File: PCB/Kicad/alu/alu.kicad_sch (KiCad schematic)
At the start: 2 parts

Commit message: Update
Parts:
- removed REF2, REF3: ~, mALUch_lib:PinHeader_2x20_P2.54mm_Horizontal, symbol mALUch_lib:2x20_2.54_Horizontal
- added J1: Conn_02x10_Odd_Even, symbol Connector_Generic:Conn_02x10_Odd_Even
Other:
- removed sheet 16b AND
- removed sheet 16b LSL
- removed sheet 16b LSR
- removed sheet 16b NOT
- removed sheet 16b OR
- removed sheet 16b XOR
- removed sheet 16b fulladder
- removed sheet 16b fulladder1
- removed sheet ALU MUX
- added sheet ADD_SUB (ADD_SUB.kicad_sch)
- added sheet AND (AND.kicad_sch)
- added sheet DECODE (DECODE.kicad_sch)
- added sheet NOT (NOT.kicad_sch)
- added sheet OR (OR.kicad_sch)
- added sheet OUT_EN (OUT_EN.kicad_sch)
- added sheet REGISTER (REGISTER.kicad_sch)
- added sheet SHIFT_REG (SHIFT_REG.kicad_sch)
- added sheet XOR (XOR.kicad_sch)
- company: AGH Logic Unit -> (none)
- title: Arithmetic Logic Unit -> (none)

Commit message: UPDATE
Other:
- sheet DECODE ports: added OP[0..3], ~{EN}, ~{REG_LOAD}, ~{SEL_ADD}, ~{SEL_AND}, ~{SEL_NOT}, ~{SEL_OR}, ~{SEL_SHL}, ~{SEL_SHR}, ~{SEL_SUB}, ~{SEL_XOR}; removed none
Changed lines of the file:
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@@
 	)
 	(sheet
-		(at 82.55 93.98)
-		(size 12.7 3.81)
+		(at 105.41 83.82)
+		(size 12.7 50.8)
 		(exclude_from_sim no)
 		(in_bom yes)
@@
 		)
 		(property "Sheetname" "DECODE"
-			(at 82.55 93.2684 0)
+			(at 105.41 83.1084 0)
 			(effects
 				(font
@@
 		)
 		(property "Sheetfile" "DECODE.kicad_sch"
-			(at 82.55 98.3746 0)
+			(at 105.41 135.2046 0)
 			(effects
 				(font
@@
 				)
 				(justify left top)
+			)
+		)
+		(pin "OP[0..3]" input
+			(at 105.41 85.09 180)
+			(effects
+				(font
+					(size 1.27 1.27)
+				)
+				(justify left)
+			)
+		)
+		(pin "~{EN}" input
+			(at 105.41 88.9 180)
+			(effects
+				(font
+					(size 1.27 1.27)
+				)
+				(justify left)
+			)
+		)
+		(pin "~{REG_LOAD}" output
+			(at 118.11 133.35 0)
+			(effects
+				(font
+					(size 1.27 1.27)
+				)
+				(justify right)
+			)
+		)
+		(pin "~{SEL_ADD}" output
+			(at 118.11 121.92 0)
+			(effects
+				(font
+					(size 1.27 1.27)
+				)
+				(justify right)
+			)
+		)
+		(pin "~{SEL_AND}" output
+			(at 118.11 106.68 0)
+			(effects
+				(font
+					(size 1.27 1.27)
+				)
+				(justify right)
+			)
+		)
+		(pin "~{SEL_NOT}" output
+			(at 118.11 110.49 0)
+			(effects
+				(font
+					(size 1.27 1.27)
+				)
+				(justify right)
+			)
+		)
+		(pin "~{SEL_OR}" output
+			(at 118.11 102.87 0)
+			(effects
+				(font
+					(size 1.27 1.27)
+				)
+				(justify right)
+			)
+		)
+		(pin "~{SEL_SHL}" output
+			(at 118.11 125.73 0)
+			(effects
+				(font
+					(size 1.27 1.27)
+				)
+				(justify right)
+			)
+		)
+		(pin "~{SEL_SHR}" output
+			(at 118.11 129.54 0)
+			(effects
+				(font
+					(size 1.27 1.27)
+				)
+				(justify right)
+			)
+		)
+		(pin "~{SEL_SUB}" output
+			(at 118.11 118.11 0)
+			(effects
+				(font
+					(size 1.27 1.27)
+				)
+				(justify right)
+			)
+		)
+		(pin "~{SEL_XOR}" output
+			(at 118.11 114.3 0)
+			(effects
+				(font
+					(size 1.27 1.27)
+				)
+				(justify right)
 			)
 		)
@@
 	)
 	(sheet
-		(at 81.28 46.99)
+		(at 105.41 40.64)
 		(size 17.78 15.24)
 		(exclude_from_sim no)
@@
 		)
 		(property "Sheetname" "REGISTER"
-			(at 81.28 46.2784 0)
+			(at 105.41 39.9284 0)
 			(effects
 				(font
@@
 		)
 		(property "Sheetfile" "REGISTER.kicad_sch"
-			(at 81.28 62.8146 0)
+			(at 105.41 56.4646 0)
 			(effects
 				(font
@@
 		)
 		(pin "CLK" input
-			(at 81.28 53.34 180)
+			(at 105.41 46.99 180)
 			(effects
 				(font
@@
 		)
 		(pin "REG_IN[0..15]" input
-			(at 81.28 49.53 180)
+			(at 105.41 43.18 180)
 			(effects
 				(font
@@
 		)
 		(pin "REG_OUT[0..15]" output
-			(at 99.06 59.69 0)
+			(at 123.19 53.34 0)
 			(effects
 				(font
@@
 		)
 		(pin "~{REG_EN}" input
-			(at 81.28 57.15 180)
+			(at 105.41 50.8 180)
 			(effects
 				(font
@@
 	)
 	(sheet
-		(at 81.28 68.58)
+		(at 105.41 62.23)
 		(size 12.7 15.24)
 		(exclude_from_sim no)
@@
 		)
 		(property "Sheetname" "OUT_EN"
-			(at 81.28 67.8684 0)
+			(at 105.41 61.5184 0)
 			(effects
 				(font
@@
 		)
 		(property "Sheetfile" "OUT_EN.kicad_sch"
-			(at 81.28 84.4046 0)
+			(at 105.41 78.0546 0)
 			(effects
 				(font
@@
 		)
 		(pin "IN[0..15]" input
-			(at 81.28 71.12 180)
+			(at 105.41 64.77 180)
 			(effects
 				(font
@@
 		)
 		(pin "OUT[0..15]" output
-			(at 93.98 81.28 0)
+			(at 118.11 74.93 0)
 			(effects
 				(font
@@
 		)
 		(pin "~{CE}" input
-			(at 81.28 74.93 180)
-			(effects
-				(font
+			(at 105.41 68.58 180)
+			(effects
+				(font

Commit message: UPDATE
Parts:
- added J2: Conn_02x10_Odd_Even, symbol Connector_Generic:Conn_02x10_Odd_Even
- added U51: 74LS04, symbol 74xx:74LS04
- added U68: 74LS08, symbol 74xx:74LS08
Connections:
- net ADD_SUB/IS_SUB: now also U51.12
- net SHIFT_REG/REV: now also U51.10
- net PWR: now reaches J1.1 (Pin_1)
- net PWR: now also J1.19 (Pin_19), J2.1 (Pin_1), J2.19 (Pin_19)
- net GND: now reaches J1.10 (Pin_10)
- net GND: now also J1.12 (Pin_12), J1.16 (Pin_16), J1.2 (Pin_2), J1.20 (Pin_20), J1.6 (Pin_6), J2.14 (Pin_14), J2.16 (Pin_16), J2.2 (Pin_2), J2.20 (Pin_20), J2.8 (Pin_8), U51.7 (GND), U68.7 (GND)
- net D11: now reaches J1.11 (Pin_11)
- net D10: now reaches J1.13 (Pin_13)
- net OP1: now reaches J1.14 (Pin_14)
- net D09: now reaches J1.15 (Pin_15)
- net D08: now reaches J1.17 (Pin_17)
- net OP0: now reaches J1.18 (Pin_18)
- net D15: now reaches J1.3 (Pin_3)
- net OP3: now reaches J1.4 (Pin_4)
- net D14: now reaches J1.5 (Pin_5)
- net D13: now reaches J1.7 (Pin_7)
- net OP2: now reaches J1.8 (Pin_8)
- net D12: now reaches J1.9 (Pin_9)
- new net CLK: J2.18 (Pin_18)
- new net D00: J2.17 (Pin_17)
- new net D01: J2.15 (Pin_15)
- new net D02: J2.13 (Pin_13)
- new net D03: J2.11 (Pin_11)
- new net D04: J2.9 (Pin_9)
- new net D05: J2.7 (Pin_7)
- new net D06: J2.5 (Pin_5)
- new net D07: J2.3 (Pin_3)
- new net FC: J2.10 (Pin_10)
- new net FO: J2.6 (Pin_6)
- new net FS: J2.4 (Pin_4)
- new net FZ: J2.12 (Pin_12)
- new net VCC: U51.14 (VCC), U68.14 (VCC)
- new net ~{SEL_ADD_SUB}: U68.11
- new net ~{SEL_ADD}: U68.13
- new net ~{SEL_SHIFT}: U68.8
- new net ~{SEL_SHL}: U68.9
- new net ~{SEL_SHR}: U51.11, U68.10
- new net ~{SEL_SUB}: U51.13, U68.12
- no-connect marks 0 -> 14
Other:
- sheet REGISTER renamed REG_A
- added sheet GATE_ADD (OUT_EN.kicad_sch)
- added sheet GATE_AND (OUT_EN.kicad_sch)
- added sheet GATE_NOT (OUT_EN.kicad_sch)
- added sheet GATE_OR (OUT_EN.kicad_sch)
- added sheet GATE_SHIFT (OUT_EN.kicad_sch)
- added sheet GATE_XOR (OUT_EN.kicad_sch)
- added sheet REG_B (REGISTER.kicad_sch)
- sheet DECODE ports: added ~{LOAD_A_REG}, ~{LOAD_B_REG}; removed ~{REG_LOAD}
- note added: "Verify the shift direction"
- moved on the sheet: J1

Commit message: UPDATE
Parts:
- removed U51: 74LS04, symbol 74xx:74LS04
- added C1: 10n, symbol Device:C
- added D1: Green LED, symbol Device:LED
- added D2, D3, D4, D5: Yellow LED, symbol Device:LED
- added R1, R2, R3, R4, R5: 680, symbol Device:R
- added U9: 74LS04, symbol 74xx:74LS04
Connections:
- net FS is gone; now on net D15: J2.4 (Pin_4)
- net PWR is gone; now on net VCC: J1.1 (Pin_1), J1.19 (Pin_19), J2.1 (Pin_1), J2.19 (Pin_19)
- net D15: now also R4.1
- net FC: now also R5.1
- net FO: now also R2.1
- net FZ: now also R3.1
- net GND: now also C1.2, D1.1 (K), D2.1 (K), D3.1 (K), D4.1 (K), D5.1 (K)
- net SHIFT_REG/REV: now also U9.12
- net VCC: now also C1.1, R1.1
- net ~{SEL_SHR}: now also U9.13
- net ~{SEL_SUB}: now also U9.11
- net D00 renamed D0
- net D01 renamed D1
- net D02 renamed D2
- net D03 renamed D3
- net D04 renamed D4
- net D05 renamed D5
- net D06 renamed D6
- net D07 renamed D7
- net D08 renamed D8
- net D09 renamed D9
- new net: D3.2 (A), R3.2
- new net: D4.2 (A), R4.2
- new net: D2.2 (A), R2.2
- new net: D5.2 (A), R5.2
- new net: D1.2 (A), R1.2
- new net IS_SUB: U9.10
- no-connect marks 14 -> 6
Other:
- removed sheet OUT_EN
- added sheet FO_FZ (OVERFLOW_FLAG.kicad_sch)
- sheet ADD_SUB ports: added FC; removed none
- moved on the sheet: J1, J2, U68E

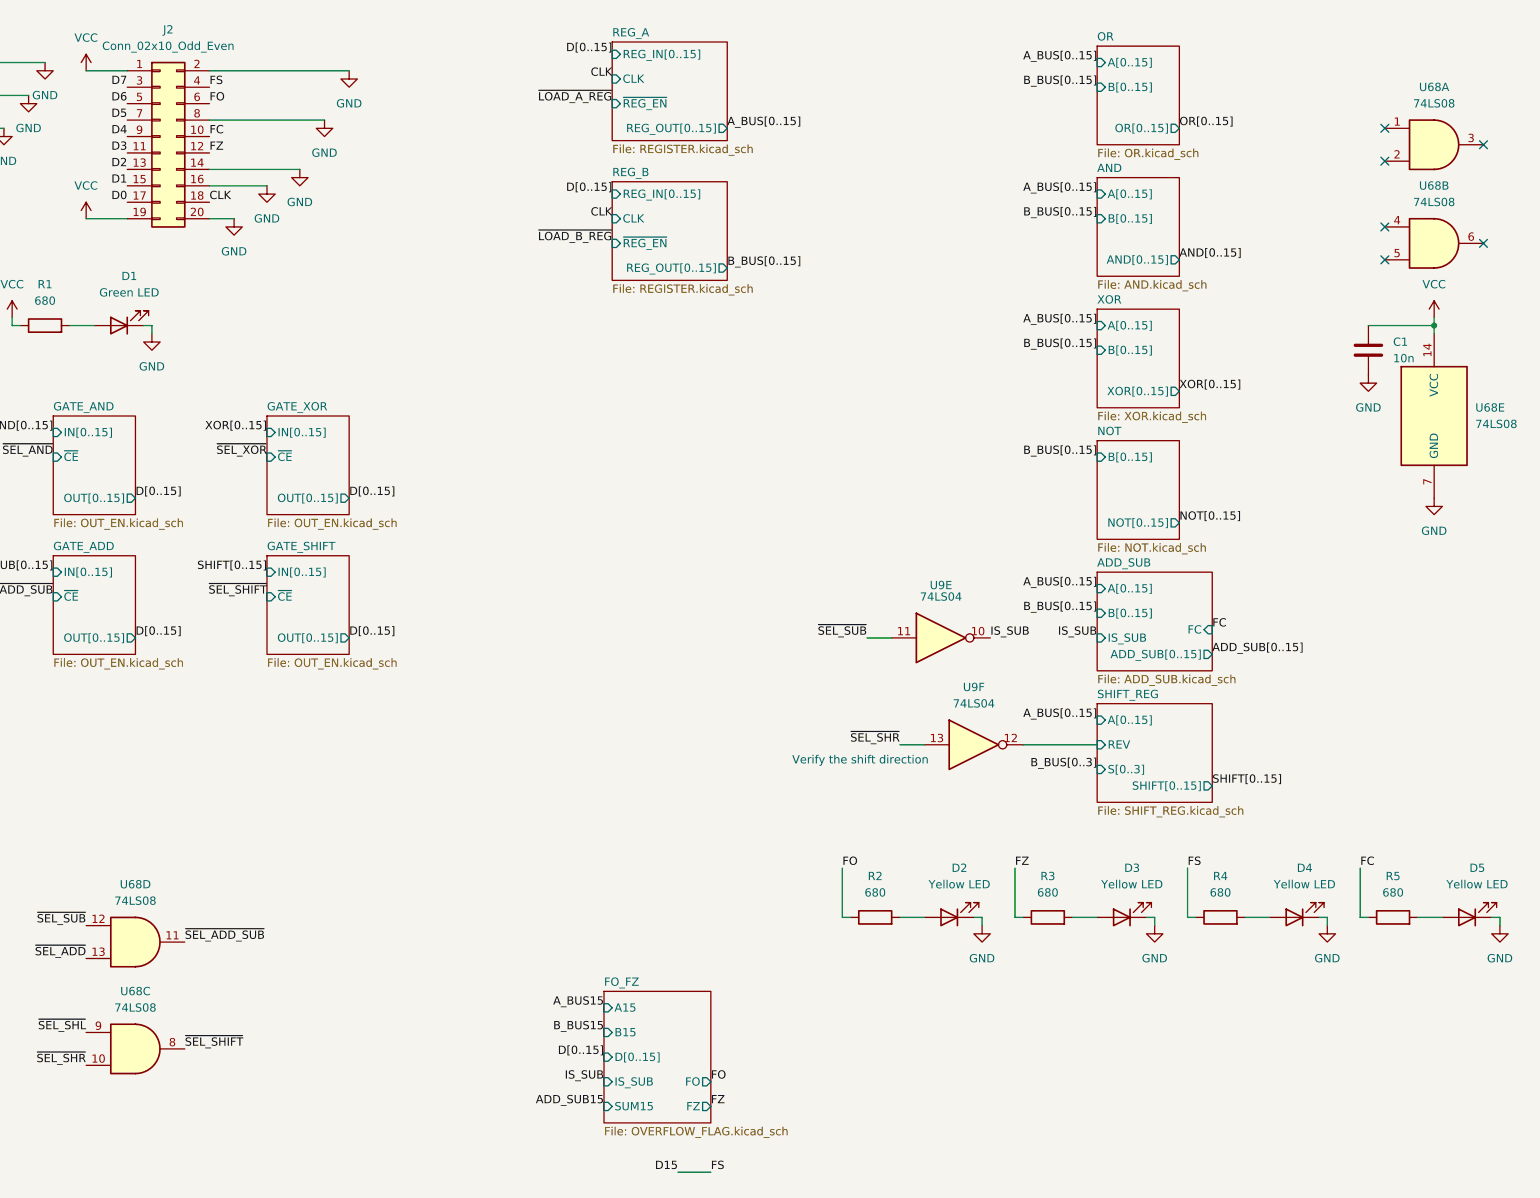
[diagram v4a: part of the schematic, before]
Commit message: LEDs added
REGISTER.kicad_sch LEDs added to both REG_A and REG_B
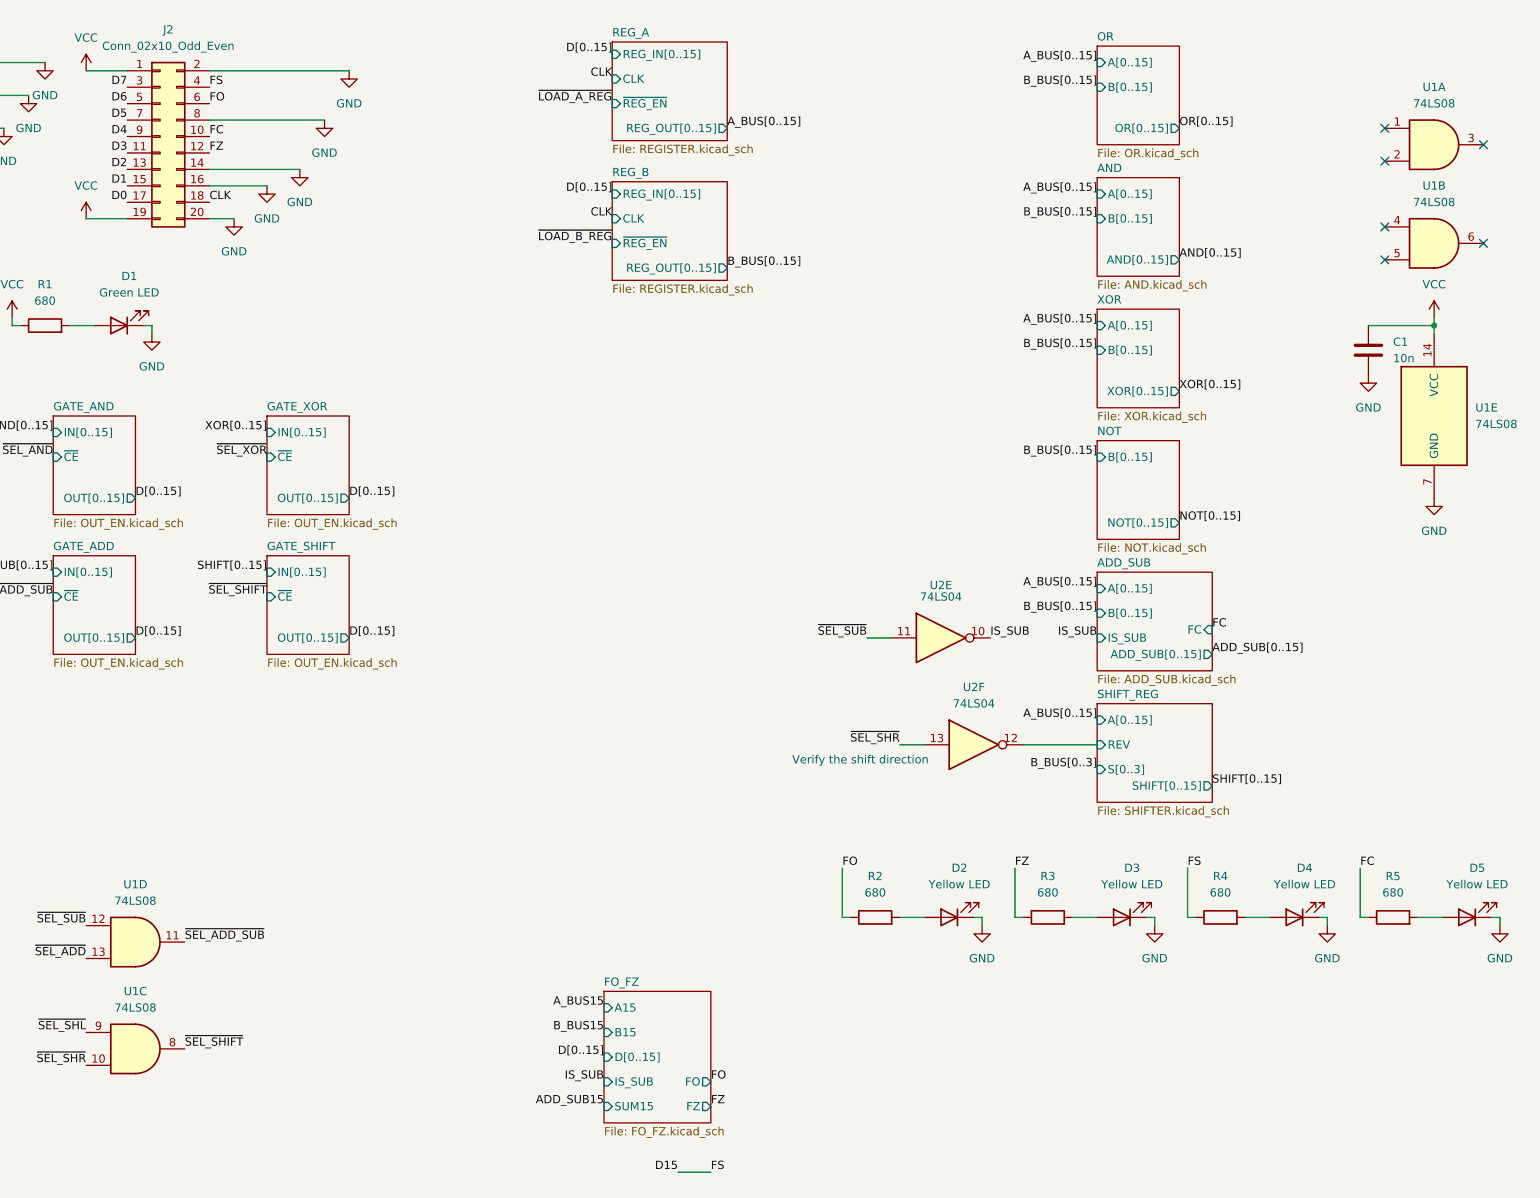
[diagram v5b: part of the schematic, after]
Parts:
- renumbered U68 to U1, U9 to U2
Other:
- sheet FO_FZ: file OVERFLOW_FLAG.kicad_sch -> FO_FZ.kicad_sch
- sheet SHIFT_REG: file SHIFT_REG.kicad_sch -> SHIFTER.kicad_sch

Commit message: Footprints, PCB update
Added footprints to all components, updated the PCB with the schematic
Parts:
- C1: footprint (none) -> Capacitor_SMD:C_0603_1608Metric
- D1, D2, D3, D4, D5: footprint (none) -> LED_SMD:LED_0603_1608Metric
- J1, J2: footprint (none) -> Connector_PinHeader_2.54mm:PinHeader_2x10_P2.54mm_Horizontal
- R1, R2, R3, R4, R5: footprint (none) -> Resistor_SMD:R_0402_1005Metric
- U1, U2: footprint (none) -> Package_SO:SOIC-14_3.9x8.7mm_P1.27mm
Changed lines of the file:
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@@
 			)
 		)
-		(property "Footprint" ""
+		(property "Footprint" "Resistor_SMD:R_0402_1005Metric"
 			(at 210.82 154.178 90)
 			(effects
@@
 			)
 		)
-		(property "Footprint" ""
+		(property "Footprint" "LED_SMD:LED_0603_1608Metric"
 			(at 248.92 152.4 0)
 			(effects
@@
 			)
 		)
-		(property "Footprint" ""
+		(property "Footprint" "Resistor_SMD:R_0402_1005Metric"
 			(at 184.15 154.178 90)
 			(effects
@@
 			)
 		)
-		(property "Footprint" ""
+		(property "Footprint" "LED_SMD:LED_0603_1608Metric"
 			(at 275.59 152.4 0)
 			(effects
@@
 			)
 		)
-		(property "Footprint" ""
+		(property "Footprint" "Package_SO:SOIC-14_3.9x8.7mm_P1.27mm"
 			(at 69.85 172.72 0)
 			(effects
@@
 			)
 		)
-		(property "Footprint" ""
+		(property "Footprint" "Package_SO:SOIC-14_3.9x8.7mm_P1.27mm"
 			(at 270.51 33.02 0)
 			(effects
@@
 			)
 		)
-		(property "Footprint" ""
+		(property "Footprint" "LED_SMD:LED_0603_1608Metric"
 			(at 222.25 152.4 0)
 			(effects
@@
 			)
 		)
-		(property "Footprint" ""
+		(property "Footprint" "Connector_PinHeader_2.54mm:PinHeader_2x10_P2.54mm_Horizontal"
 			(at 73.66 31.75 0)
 			(effects
@@
 			)
 		)
-		(property "Footprint" ""
+		(property "Footprint" "Package_SO:SOIC-14_3.9x8.7mm_P1.27mm"
 			(at 194.31 109.22 0)
 			(effects
@@
 			)
 		)
-		(property "Footprint" ""
+		(property "Footprint" "Package_SO:SOIC-14_3.9x8.7mm_P1.27mm"
 			(at 270.51 74.93 0)
 			(effects
@@
 			)
 		)
-		(property "Footprint" ""
+		(property "Footprint" "Package_SO:SOIC-14_3.9x8.7mm_P1.27mm"
 			(at 69.85 156.21 0)
 			(effects
@@
 			)
 		)
-		(property "Footprint" ""
+		(property "Footprint" "Resistor_SMD:R_0402_1005Metric"
 			(at 237.49 154.178 90)
 			(effects
@@
 			)
 		)
-		(property "Footprint" ""
+		(property "Footprint" "Package_SO:SOIC-14_3.9x8.7mm_P1.27mm"
 			(at 270.51 48.26 0)
 			(effects
@@
 			)
 		)
-		(property "Footprint" ""
+		(property "Footprint" "Package_SO:SOIC-14_3.9x8.7mm_P1.27mm"
 			(at 199.39 125.73 0)
 			(effects
@@
 			)
 		)
-		(property "Footprint" ""
+		(property "Footprint" "LED_SMD:LED_0603_1608Metric"
 			(at 67.31 60.96 0)
 			(effects
@@
 			)
 		)
-		(property "Footprint" ""
+		(property "Footprint" "LED_SMD:LED_0603_1608Metric"
 			(at 195.58 152.4 0)
 			(effects
@@
 			)
 		)
-		(property "Footprint" ""
+		(property "Footprint" "Resistor_SMD:R_0402_1005Metric"
 			(at 55.88 62.738 90)
 			(effects
@@
 			)
 		)
-		(property "Footprint" ""
+		(property "Footprint" "Resistor_SMD:R_0402_1005Metric"
 			(at 264.16 154.178 90)
 			(effects
@@
 			)
 		)
-		(property "Footprint" ""
+		(property "Footprint" "Capacitor_SMD:C_0603_1608Metric"
 			(at 261.3152 68.58 0)
 			(effects
@@
 			)
 		)
-		(property "Footprint" ""
+		(property "Footprint" "Connector_PinHeader_2.54mm:PinHeader_2x10_P2.54mm_Horizontal"
 			(at 27.94 30.48 0)
 			(effects

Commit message: ALU Pcb update
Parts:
- added H1, H2, H3, H4: MountingHole_Pad, MountingHole:MountingHole_2.2mm_M2_DIN965_Pad, symbol Mechanical:MountingHole_Pad
- C1: value 10n -> 100nF; footprint Capacitor_SMD:C_0603_1608Metric -> Capacitor_SMD:C_0402_1005Metric
- D1: value Green LED -> green
- D2, D3, D4, D5: value Yellow LED -> Yellow
- J1, J2: value Conn_02x10_Odd_Even -> out; footprint Connector_PinHeader_2.54mm:PinHeader_2x10_P2.54mm_Horizontal -> mALUch_lib:PinHeader_2x10_P2.54mm_Horizontal
- U1: value 74LS08 -> 7408; footprint Package_SO:SOIC-14_3.9x8.7mm_P1.27mm -> Package_SO:SO-14_3.9x8.65mm_P1.27mm
- U2: value 74LS04 -> 7404; footprint Package_SO:SOIC-14_3.9x8.7mm_P1.27mm -> Package_SO:SO-14_3.9x8.65mm_P1.27mm
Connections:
- net CLK: now also J2.4 (Pin_4); no longer J2.18 (Pin_18)
- net D0: now also J2.3 (Pin_3); no longer J2.17 (Pin_17)
- net D1: now also J2.5 (Pin_5); no longer J2.15 (Pin_15)
- net D10: now also J1.7 (Pin_7); no longer J1.13 (Pin_13)
- net D11: now also J1.9 (Pin_9); no longer J1.11 (Pin_11)
- net D12: now also J1.11 (Pin_11); no longer J1.9 (Pin_9)
- net D13: now also J1.13 (Pin_13); no longer J1.7 (Pin_7)
- net D14: now also J1.15 (Pin_15); no longer J1.5 (Pin_5)
- net D15: now also J1.17 (Pin_17), J2.18 (Pin_18); no longer J1.3 (Pin_3), J2.4 (Pin_4)
- net D2: now also J2.7 (Pin_7); no longer J2.13 (Pin_13)
- net D3: now also J2.9 (Pin_9); no longer J2.11 (Pin_11)
- net D4: now also J2.11 (Pin_11); no longer J2.9 (Pin_9)
- net D5: now also J2.13 (Pin_13); no longer J2.7 (Pin_7)
- net D6: now also J2.15 (Pin_15); no longer J2.5 (Pin_5)
- net D7: now also J2.17 (Pin_17); no longer J2.3 (Pin_3)
- net D8: now also J1.3 (Pin_3); no longer J1.17 (Pin_17)
- net D9: now also J1.5 (Pin_5); no longer J1.15 (Pin_15)
- net FC: now also J2.12 (Pin_12); no longer J2.10 (Pin_10)
- net FO: now also J2.16 (Pin_16); no longer J2.6 (Pin_6)
- net FZ: now also J2.10 (Pin_10); no longer J2.12 (Pin_12)
- net GND: now also J2.6 (Pin_6), H1.1, H2.1, H3.1, H4.1; no longer J2.16 (Pin_16)
- net OP0: now also J1.4 (Pin_4); no longer J1.18 (Pin_18)
- net OP1: now also J1.8 (Pin_8); no longer J1.14 (Pin_14)
- net OP2: now also J1.14 (Pin_14); no longer J1.8 (Pin_8)
- net OP3: now also J1.18 (Pin_18); no longer J1.4 (Pin_4)
